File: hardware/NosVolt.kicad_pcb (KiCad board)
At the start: 4 copper layers, 112.8 x 113.6 mm, 100 parts, among them CN201 100nF, J101 INPUTS, J102 OUTPUTS, J401 USB_C_Receptacle_USB2.0_16P, Q1101 2N7002, Q1102 AO4407A, Q801 2N7002, Q802 AO4407A, Q901 2N7002, Q902 AO4407A, SW101 SW_Reset, SW102 SSSS811101, U1001 INA226, U101 ESP32-S3-WROOM-1, U1201 INA226, U201 ADS1115IDGS, U301 MP2307DN-LF-Z, U401 AP7361-33ER-13, U402 USBLC6-2SC6, U501 INA226, U601 INA226, U701 INA226

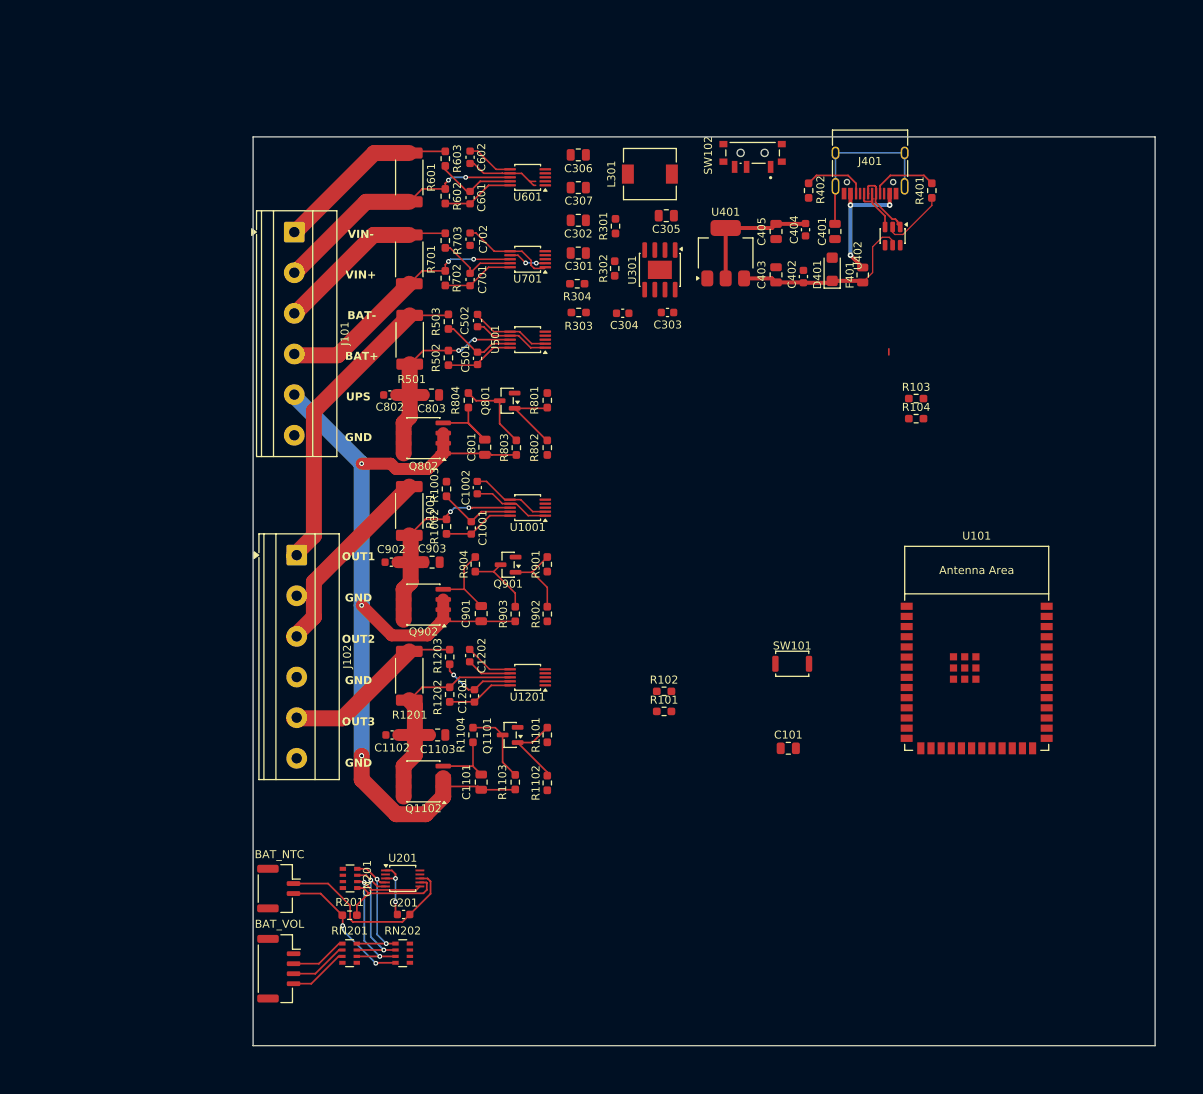
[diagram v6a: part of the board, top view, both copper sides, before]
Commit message: ldo optimization
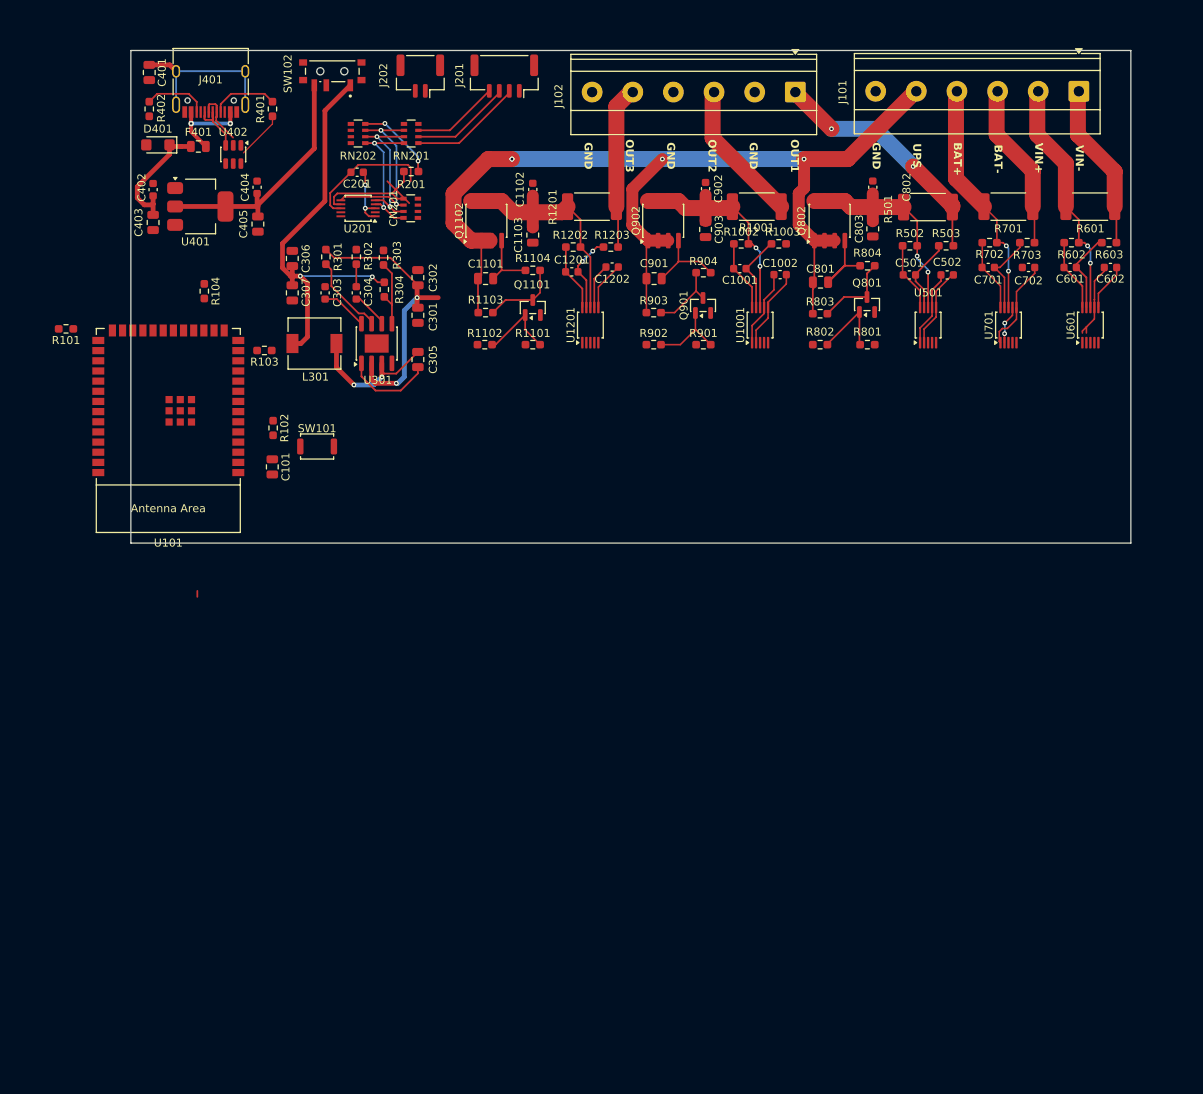
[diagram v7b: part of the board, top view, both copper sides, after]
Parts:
- removed BAT_NTC: BAT_NTC, Connector_JST:JST_GH_SM02B-GHS-TB_1x02-1MP_P1.25mm_Horizontal
- removed BAT_VOL: BAT_SENSE, Connector_JST:JST_GH_SM04B-GHS-TB_1x04-1MP_P1.25mm_Horizontal
- added J201: BAT_SENSE, Connector_JST:JST_GH_SM04B-GHS-TB_1x04-1MP_P1.25mm_Horizontal, F.Cu at (138.8, 42.2)
- added J202: BAT_NTC, Connector_JST:JST_GH_SM02B-GHS-TB_1x02-1MP_P1.25mm_Horizontal, F.Cu at (128.3, 42.2)
- moved U101 106.4 mm to (96.8, 83.5), turned to 180 degrees
- moved RN201 102.7 mm to (127.2, 49.4), turned to 180 degrees
- moved RN202 102.6 mm to (120.5, 49.4), turned to 180 degrees
- moved J101 99.6 mm to (210.6, 44.1), turned to 180 degrees
- moved R201 93.3 mm to (127.2, 54.1), turned to 0 degrees
- moved C201 93.0 mm to (120.4, 54.2), turned to 0 degrees
- moved R104 90.4 mm to (101.3, 69.1), turned to -90 degrees
- moved R101 88.7 mm to (84.0, 73.8), turned to 180 degrees
- moved C401 88.0 mm to (94.4, 41.8)
- moved D401 85.7 mm to (95.5, 50.8), turned to 180 degrees
- moved R601 85.2 mm to (212.1, 58.5), turned to 180 degrees
- moved J102 85.1 mm to (175.2, 44.2), turned to 180 degrees
- moved F401 84.6 mm to (100.6, 51.0), turned to 180 degrees
- moved CN201 84.1 mm to (127.1, 58.7), turned to 0 degrees
- moved U201 84.0 mm to (120.5, 58.7), turned to 180 degrees
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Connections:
- SW102 pad 1: /USB_LDO/3V3 -> /MP2307/OUT
- SW102 pad 3: /MP2307/OUT -> /USB_LDO/3V3
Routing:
- net /MP2307/OUT: track 0.00 -> 52.6 mm, vias 0 -> 2
- net +12V_UPS: track 122.9 -> 164.4 mm, vias 4 -> 6
- net Net-(U301-SW): track 0.00 -> 18.4 mm, vias 0 -> 2
- net /USB_LDO/3V3: track 17.3 -> 31.3 mm
- net Net-(U301-BS): track 0.00 -> 11.1 mm
- net Net-(U301-EN): track 0.00 -> 10.2 mm
- net /Output1/VOUT: track 41.0 -> 30.9 mm, vias 0 -> 2
- net Net-(U301-FB): track 0.00 -> 9.13 mm
- net +3.3V: track 68.7 -> 60.5 mm
- net /USB_LDO/5V: track 23.9 -> 15.8 mm
- net Net-(J202-Pin_2): track 17.4 -> 10.2 mm
- net BAT_1: track 7.14 -> 14.2 mm
- net /Output2/VOUT: track 24.8 -> 18.0 mm
- net Net-(U301-SS): track 0.00 -> 5.82 mm
- net BAT_2: track 7.33 -> 12.6 mm
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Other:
- board size 112.8 x 113.6 mm -> 125 x 61.6 mm

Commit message: Add screen
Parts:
- added U102: GMT028-05, NosLib:GMT028-05, B.Cu at (173.2, 71.3)
- moved C401 176.0 mm to (261.4, 97.5)
- moved R101 172.3 mm to (251.5, 114.2)
- moved R103 172.3 mm to (276.3, 116.9)
- moved R104 172.3 mm to (268.8, 109.5)
- moved C101 137.0 mm to (242.5, 125.2)
- moved R102 137.0 mm to (242.6, 120.4)
- moved SW101 137.0 mm to (248.1, 122.7)
- moved U101 134.0 mm to (229.5, 64.7), turned to -90 degrees
- moved R402 124.8 mm to (219.1, 42.6)
- moved R401 124.7 mm to (234.4, 42.6)
- moved J401 124.6 mm to (226.7, 41.8)
- moved D401 121.1 mm to (216.6, 53.4), turned to -90 degrees
- moved U402 120.8 mm to (225.7, 50.8)
- moved C403 118.4 mm to (212.7, 48.8), turned to 90 degrees
- moved C402 117.8 mm to (212.7, 53.0), turned to -90 degrees
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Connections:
- net /USB_LDO/5V renamed /USB_LDO/USB_5V
- C404 pad 1: /USB_LDO/3V3 -> /USB_LDO/USB_3V3
- C405 pad 1: /USB_LDO/3V3 -> /USB_LDO/USB_3V3
- J101 pad 1: /INA226_IN/VOUT -> +12V_UPS
- J101 pad 2: /INA226_IN/VIN -> GND
- J101 pad 5: +12V_UPS -> /INA226_IN/VOUT
- J101 pad 6: GND -> /INA226_IN/VIN
- SW102 pad 1: /MP2307/OUT -> unconnected-(SW102-Pad1)
- SW102 pad 2: unconnected-(SW102-Pad2) -> +3.3V
- SW102 pad 3: /USB_LDO/3V3 -> /MP2307/OUT
- U101 pad 18: unconnected-(U101-GPIO10/TOUCH10/ADC1_CH9/FSPICS0/FSPIIO4/SUBSPICS0-Pad18) -> SPI_CS_TFT
- U101 pad 19: unconnected-(U101-GPIO11/TOUCH11/ADC2_CH0/FSPID/FSPIIO5/SUBSPID-Pad19) -> SPI_MOSI
- U101 pad 20: unconnected-(U101-GPIO12/TOUCH12/ADC2_CH1/FSPICLK/FSPIIO6/SUBSPICLK-Pad20) -> SPI_SCLK
- U101 pad 21: unconnected-(U101-GPIO13/TOUCH13/ADC2_CH2/FSPIQ/FSPIIO7/SUBSPIQ-Pad21) -> TFT_DC
- U101 pad 22: unconnected-(U101-GPIO14/TOUCH14/ADC2_CH3/FSPIWP/FSPIDQS/SUBSPIWP-Pad22) -> TFT_RST
- U401 pad 2: /USB_LDO/3V3 -> /USB_LDO/USB_3V3
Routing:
- net +12V_UPS: track 164.4 -> 70.6 mm, vias 6 -> 2
- net /USB_LDO/3V3: track 31.3 -> 0.00 mm
- net /MP2307/OUT: track 52.6 -> 25.6 mm
- net /Output1/VOUT: track 30.9 -> 5.14 mm, vias 2 -> 0
- net /Output2/VOUT: track 18.0 -> 0.00 mm
- net /INA226_IN/VOUT: track 20.6 -> 4.29 mm
- net /INA226_BAT/VOUT: track 20.6 -> 4.29 mm
- net /INA226_IN/VIN: track 30.2 -> 14.3 mm
- net /INA226_BAT/VIN: track 30.2 -> 14.3 mm
- net /Output3/VOUT: track 20.3 -> 5.14 mm
- net BAT_1: track 14.2 -> 0.62 mm
- net /USB_LDO/USB_3V3: track 0.00 -> 13.3 mm
- net BAT_2: track 12.6 -> 0.42 mm
- net /USB_LDO/RAW_5V: track 11.4 -> 0.00 mm, vias 2 -> 0
- net BAT_3: track 10.9 -> 0.62 mm
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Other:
- board size 125 x 61.6 mm -> 145 x 60 mm
